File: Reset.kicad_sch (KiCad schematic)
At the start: 4 parts, among them U6 74LVC1G04

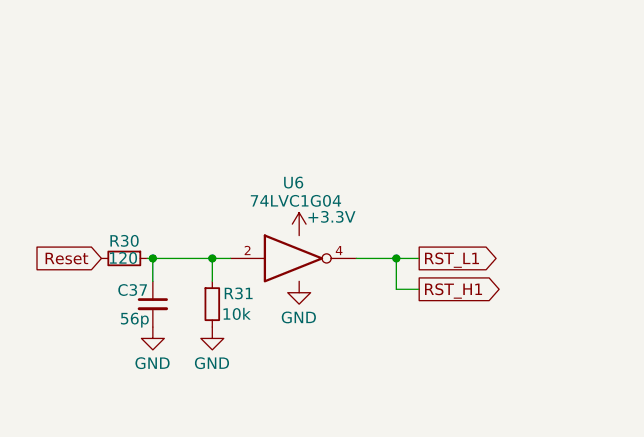
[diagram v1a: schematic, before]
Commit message: Убрал питание 3.3В
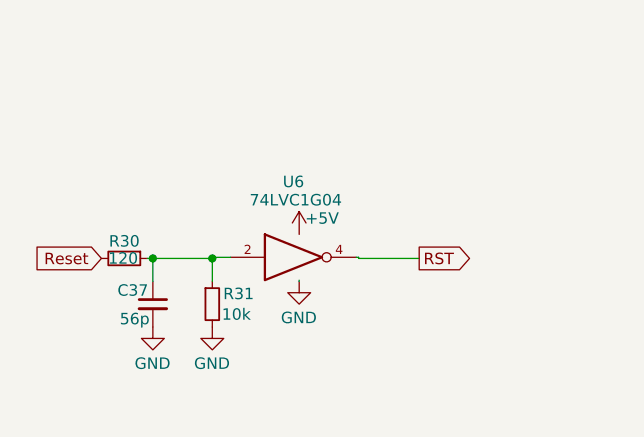
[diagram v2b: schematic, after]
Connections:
- net +3V3 renamed +5V
- net RST_H1 renamed RST

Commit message: Развел все дорожки
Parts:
- added C9: 2.2u, Capacitor_SMD:C_0805_2012Metric_Pad1.18x1.45mm_HandSolder, symbol Device:C_Small
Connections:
- net +5V: now also C9.1
- net GND: now also C9.2
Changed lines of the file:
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@@
+	(symbol
+		(lib_id "power:GND")
+		(at 139.065 73.025 0)
+		(unit 1)
+		(exclude_from_sim no)
+		(in_bom yes)
+		(on_board yes)
+		(dnp no)
+		(property "Reference" "#PWR070"
+			(at 139.065 79.375 0)
+			(effects
+				(font
+					(size 1.27 1.27)
+				)
+				(hide yes)
+			)
+		)
+		(property "Value" "GND"
+			(at 137.033 77.089 0)
+			(effects
+				(font
+					(size 1.27 1.27)
+				)
+				(justify left)
+			)
+		)
+		(property "Footprint" ""
+			(at 139.065 73.025 0)
+			(effects
+				(font
+					(size 1.27 1.27)
+				)
+				(hide yes)
+			)
+		)
+		(property "Datasheet" ""
+			(at 139.065 73.025 0)
+			(effects
+				(font
+					(size 1.27 1.27)
+				)
+				(hide yes)
+			)
+		)
+		(property "Description" ""
+			(at 139.065 73.025 0)
+			(effects
+				(font
+					(size 1.27 1.27)
+				)
+				(hide yes)
+			)
+		)
+		(pin "1"
+		)
+		(instances
+			(project "Driver_Inductor"
+				(path "/e63e39d7-6ac0-4ffd-8aa3-1841a4541b55/cb537d0a-be40-4038-86f7-62065d47d4b4"
+					(reference "#PWR070")
+					(unit 1)
+				)
+			)
+		)
+	)
 	(symbol
 		(lib_id "power:GND")
@@
 	(symbol
 		(lib_id "power:+5V")
+		(at 139.065 67.945 0)
+		(unit 1)
+		(exclude_from_sim no)
+		(in_bom yes)
+		(on_board yes)
+		(dnp no)
+		(property "Reference" "#PWR014"
+			(at 139.065 71.755 0)
+			(effects
+				(font
+					(size 1.27 1.27)
+				)
+				(hide yes)
+			)
+		)
+		(property "Value" "+5V"
+			(at 138.811 64.135 0)
+			(effects
+				(font
+					(size 1.27 1.27)
+				)
+			)
+		)
+		(property "Footprint" ""
+			(at 139.065 67.945 0)
+			(effects
+				(font
+					(size 1.27 1.27)
+				)
+				(hide yes)
+			)
+		)
+		(property "Datasheet" ""
+			(at 139.065 67.945 0)
+			(effects
+				(font
+					(size 1.27 1.27)
+				)
+				(hide yes)
+			)
+		)
+		(property "Description" "Power symbol creates a global label with name \"+5V\""
+			(at 139.065 67.945 0)
+			(effects
+				(font
+					(size 1.27 1.27)
+				)
+				(hide yes)
+			)
+		)
+		(pin "1"
+		)
+		(instances
+			(project "Driver_Inductor"
+				(path "/e63e39d7-6ac0-4ffd-8aa3-1841a4541b55/cb537d0a-be40-4038-86f7-62065d47d4b4"
+					(reference "#PWR014")
+					(unit 1)
+				)
+			)
+		)
+	)
+	(symbol
+		(lib_id "power:+5V")
 		(at 139.446 86.868 0)
 		(unit 1)
@@
 					(unit 1)
 				)
+			)
+		)
+	)
+	(symbol
+		(lib_id "Device:C_Small")
+		(at 139.065 70.485 0)
+		(unit 1)
+		(exclude_from_sim no)
+		(in_bom yes)
+		(on_board yes)
+		(dnp no)
+		(property "Reference" "C9"
+			(at 141.4018 69.3166 0)
+			(effects
+				(font
+					(size 1.27 1.27)
+				)
+				(justify left)
+			)
+		)
+		(property "Value" "2.2u"
+			(at 141.4018 71.628 0)
+			(effects
+				(font
+					(size 1.27 1.27)
+				)
+				(justify left)
+			)
+		)
+		(property "Footprint" "Capacitor_SMD:C_0805_2012Metric_Pad1.18x1.45mm_HandSolder"
+			(at 139.065 70.485 0)
+			(effects
+				(font
+					(size 1.27 1.27)
+				)
+				(hide yes)
+			)
+		)
+		(property "Datasheet" "~"
+			(at 139.065 70.485 0)
+			(effects
+				(font
+					(size 1.27 1.27)
+				)
+				(hide yes)
+			)
+		)
+		(property "Description" ""
+			(at 139.065 70.485 0)
+			(effects
+				(font
+					(size 1.27 1.27)
+				)
+				(hide yes)
+			)
+		)
+		(pin "1"
+		)
+		(pin "2"
+		)
+		(instances
+			(project "Driver_Inductor"
+				(path "/e63e39d7-6ac0-4ffd-8aa3-1841a4541b55/cb537d0a-be40-4038-86f7-62065d47d4b4"
+					(reference "C9")
+					(unit 1)
+				)

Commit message: VER2.0 Отправил в резонит
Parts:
- removed C37: 56p, Capacitor_SMD:C_0805_2012Metric_Pad1.18x1.45mm_HandSolder, symbol Device:C_Small
- removed C9: 2.2u, Capacitor_SMD:C_0805_2012Metric_Pad1.18x1.45mm_HandSolder, symbol Device:C_Small
- removed R30: 120, Resistor_SMD:R_0805_2012Metric_Pad1.20x1.40mm_HandSolder, symbol Device:R_Small
- removed R31: 10k, Resistor_SMD:R_0805_2012Metric_Pad1.20x1.40mm_HandSolder, symbol Device:R_Small
- removed U6: 74LVC1G04, Package_TO_SOT_SMD:SOT-23-5_HandSoldering, symbol 74xGxx:74LVC1G04
- added Q1: IRLML2402TRPBF, Package_TO_SOT_SMD:SOT-23, symbol Transistor_FET:2N7002
- added R24: 0, Resistor_SMD:R_0805_2012Metric_Pad1.20x1.40mm_HandSolder, symbol Device:R_Small
- added R32: 1k, Resistor_SMD:R_0805_2012Metric_Pad1.20x1.40mm_HandSolder, symbol Device:R_Small
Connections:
- net +5V: now also R32.2
- net GND: now also Q1.2 (S)
- net RST: now also Q1.3 (D), R32.1
- net Reset: now also R24.1
- new net: Q1.1 (G), R24.2

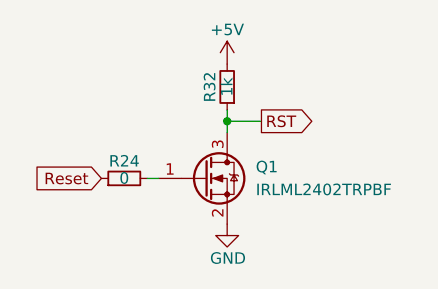
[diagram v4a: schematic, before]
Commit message: Изменения: изменил BOM, сделал заказ
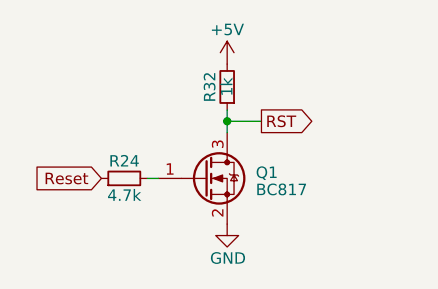
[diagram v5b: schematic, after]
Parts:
- Q1: value IRLML2402TRPBF -> BC817
- R24: value 0 -> 4.7k
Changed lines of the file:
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@@
 			)
 		)
-		(property "Value" "0"
-			(at 142.875 97.155 90)
+		(property "Value" "4.7k"
+			(at 142.875 99.06 90)
 			(effects
 				(font
@@
 		(fields_autoplaced yes)
 		(property "Reference" "Q1"
-			(at 157.48 95.8849 0)
+			(at 157.48 96.5199 0)
 			(effects
 				(font
@@
 			)
 		)
-		(property "Value" "IRLML2402TRPBF"
-			(at 157.48 98.4249 0)
+		(property "Value" "BC817"
+			(at 157.48 98.425 0)
 			(effects
 				(font
